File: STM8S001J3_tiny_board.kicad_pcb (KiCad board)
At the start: 2 copper layers, 20 x 14 mm, 10 parts, among them J1 Conn_01x05_Male, J2 Conn_01x04_Male, U1 STM8S001J3M

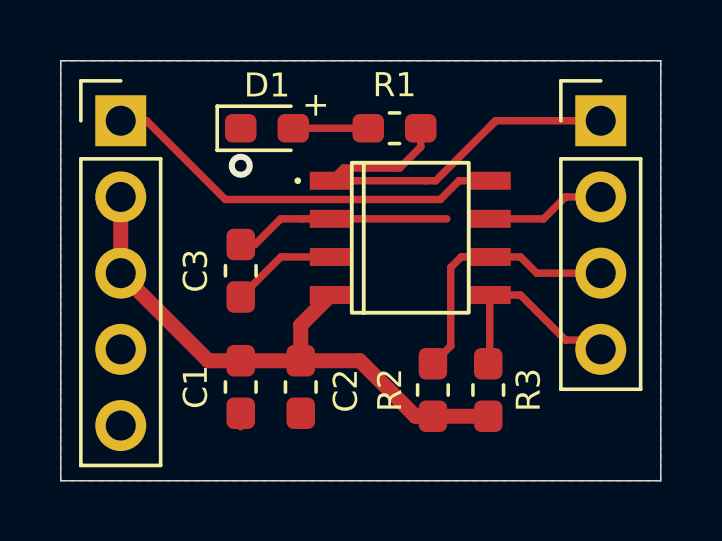
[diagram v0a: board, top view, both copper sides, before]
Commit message: Fix the traces from pin #1 of the MCU to LED and connector
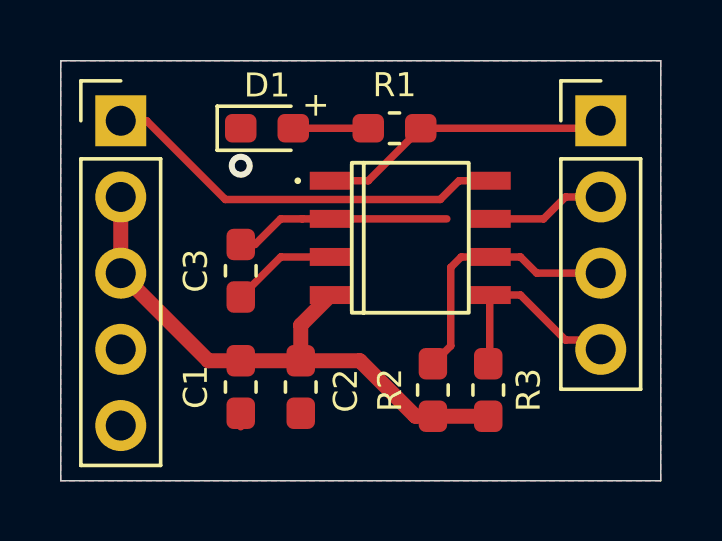
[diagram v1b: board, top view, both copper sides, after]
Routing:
- net Net-(J2-Pad1): track 15.6 -> 9.83 mm
